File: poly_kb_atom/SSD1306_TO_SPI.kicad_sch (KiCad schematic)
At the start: 12 parts

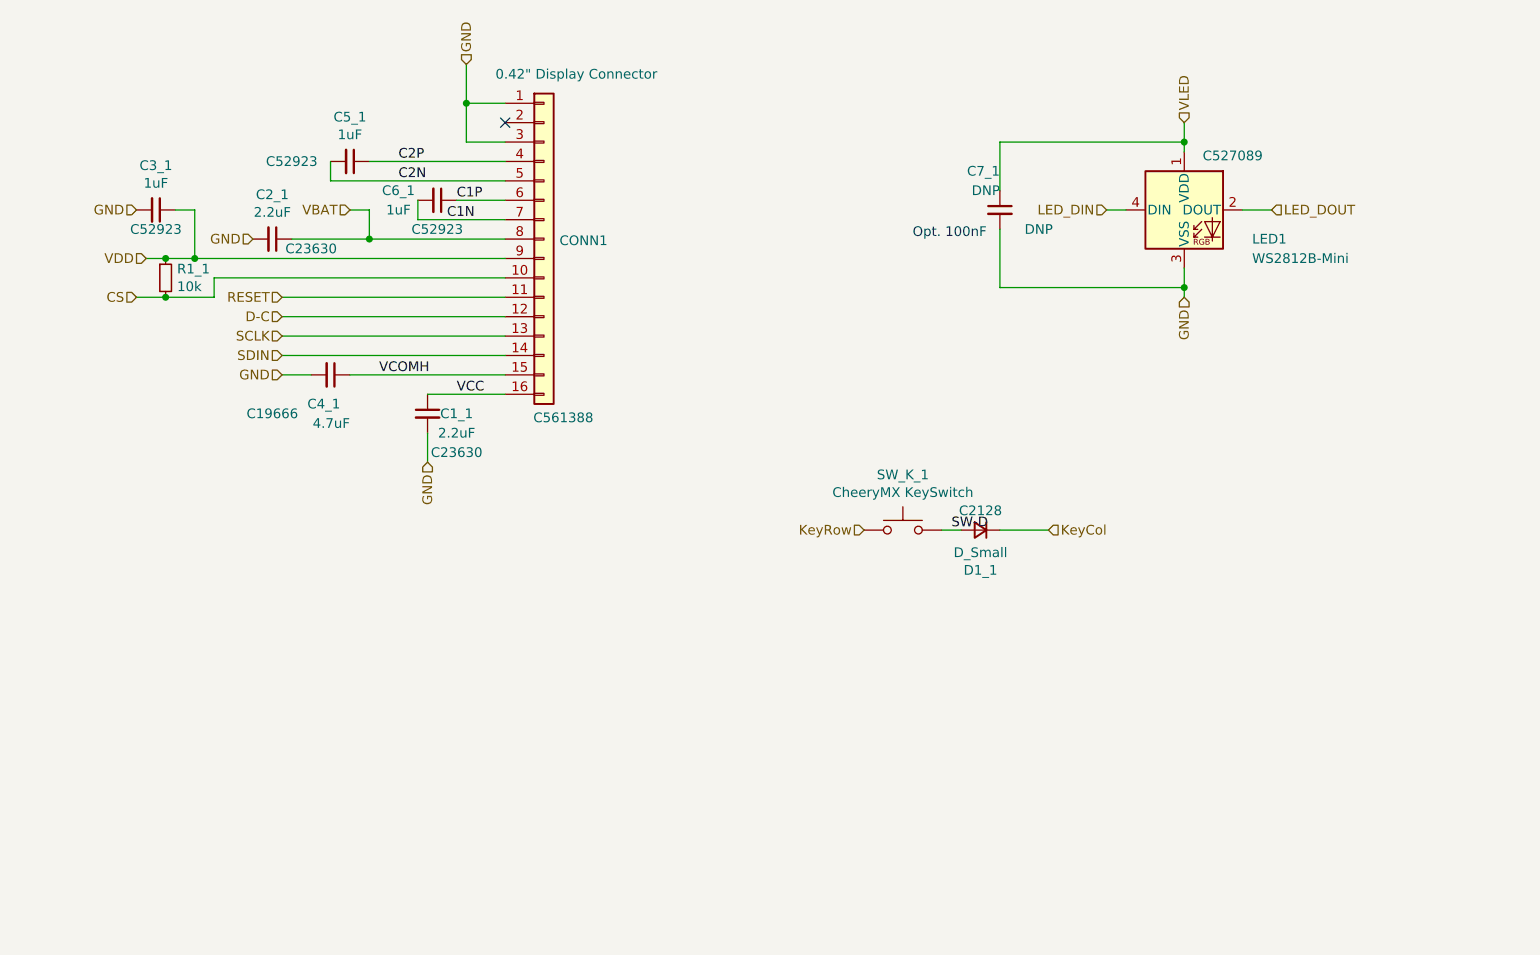
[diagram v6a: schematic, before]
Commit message: Updated WaveL to Revision 1.1
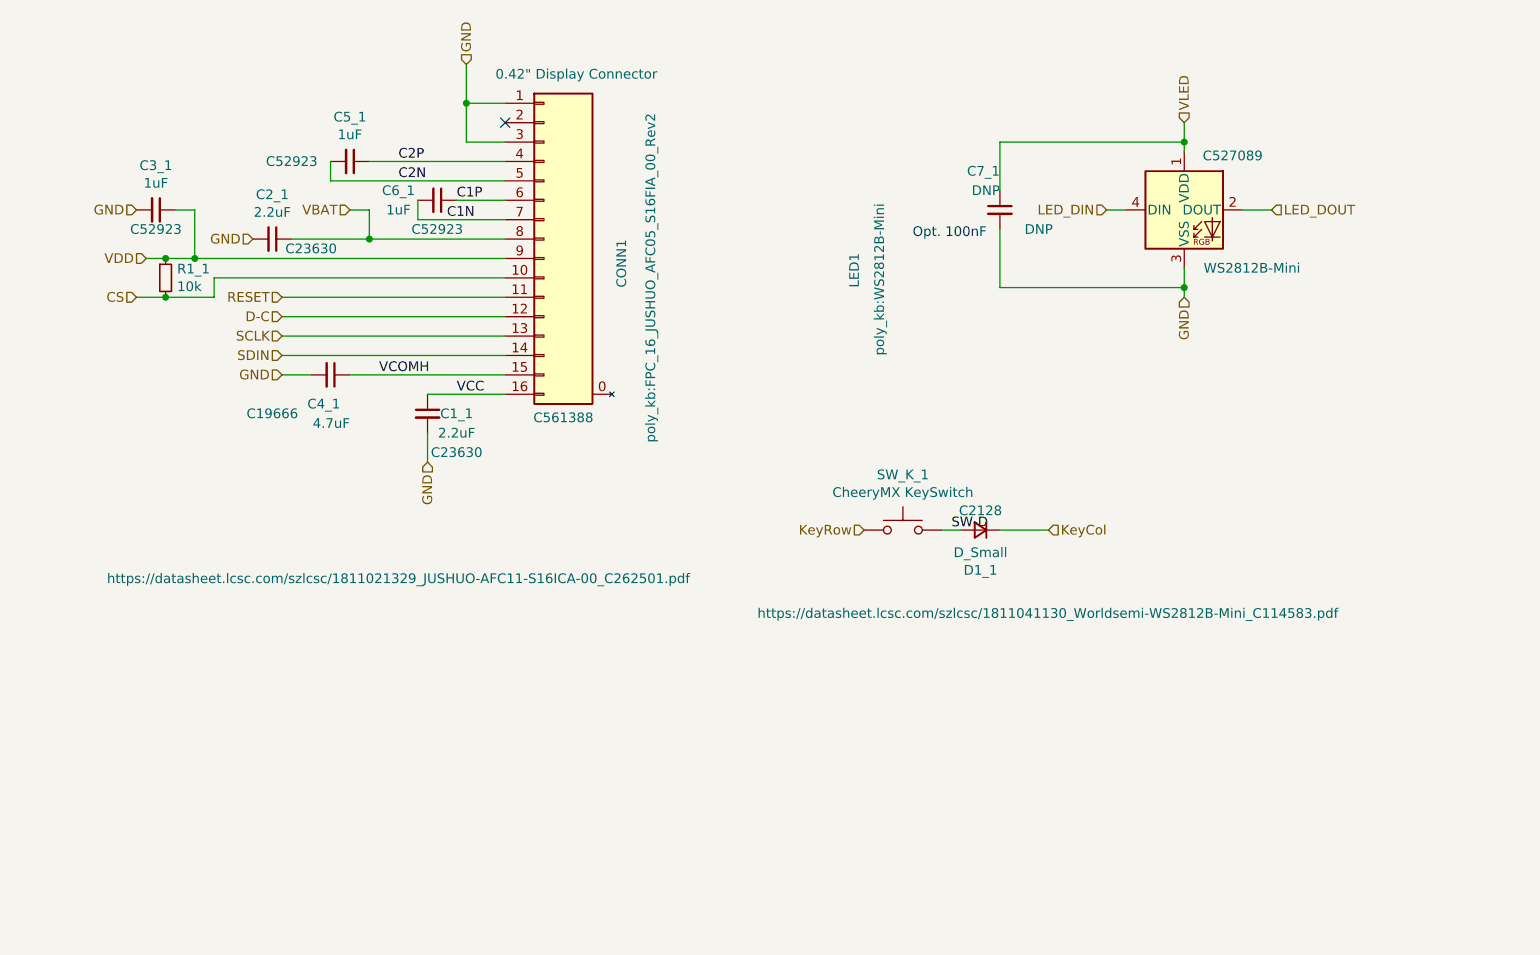
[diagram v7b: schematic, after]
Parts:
- C1_1, C2_1, C4_1, C7_1: footprint (none) -> Capacitor_SMD:C_0603_1608Metric
- C3_1, C5_1, C6_1: footprint (none) -> Capacitor_SMD:C_0402_1005Metric
- CONN1: footprint (none) -> poly_kb:FPC_16_JUSHUO_AFC05_S16FIA_00_Rev2
- D1_1: footprint (none) -> poly_kb:D_SOD-323Ext
- LED1: footprint (none) -> poly_kb:WS2812B-Mini
- R1_1: footprint (none) -> Resistor_SMD:R_0402_1005Metric
- SW_K_1: footprint (none) -> poly_kb:SW_Cherry_MX_1.00u_PCB_NoSilk
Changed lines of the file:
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@@
   (symbol (lib_id "Connector_Generic:Conn_01x16") (at 82.55 52.07 0) (unit 1)
     (in_bom yes) (on_board yes)
-    (property "Reference" "CONN1" (id 0) (at 84.582 52.2732 0)
+    (property "Reference" "CONN1" (id 0) (at 92.71 58.42 90)
       (effects (font (size 1.27 1.27)) (justify left))
     )
@@
       (effects (font (size 1.27 1.27)) (justify left))
     )
-    (property "Footprint" "" (id 2) (at 82.55 52.07 0)
-      (effects (font (size 1.27 1.27)) hide)
-    )
-    (property "Datasheet" "https://datasheet.lcsc.com/szlcsc/1811021329_JUSHUO-AFC11-S16ICA-00_C262501.pdf" (id 3) (at 82.55 52.07 0)
-      (effects (font (size 1.27 1.27)) hide)
-    )
+    (property "Footprint" "poly_kb:FPC_16_JUSHUO_AFC05_S16FIA_00_Rev2" (id 2) (at 96.52 57.15 90))
+    (property "Datasheet" "https://datasheet.lcsc.com/szlcsc/1811021329_JUSHUO-AFC11-S16ICA-00_C262501.pdf" (id 3) (at 63.5 96.52 0))
     (property "LCSC" "C561388" (id 4) (at 85.09 76.2 0)
       (effects (font (size 1.27 1.27)) (justify bottom))
@@
       (effects (font (size 1.27 1.27)) hide)
     )
+    (pin "0")
     (pin "1")
     (pin "10")
@@
     (property "Reference" "C6_1" (id 0) (at 63.5 45.72 90))
     (property "Value" "1uF" (id 1) (at 63.5 48.26 90))
-    (property "Footprint" "" (id 2) (at 68.58 46.99 0)
+    (property "Footprint" "Capacitor_SMD:C_0402_1005Metric" (id 2) (at 68.58 46.99 0)
       (effects (font (size 1.27 1.27)) hide)
     )
@@
   (symbol (lib_id "LED:WS2812B") (at 166.37 48.26 0) (unit 1)
     (in_bom yes) (on_board yes)
-    (property "Reference" "LED1" (id 0) (at 175.26 52.07 0)
-      (effects (font (size 1.27 1.27)) (justify left))
-    )
-    (property "Value" "WS2812B-Mini" (id 1) (at 175.26 54.61 0)
-      (effects (font (size 1.27 1.27)) (justify left))
-    )
-    (property "Footprint" "" (id 2) (at 167.64 55.88 0)
-      (effects (font (size 1.27 1.27)) (justify left top) hide)
-    )
-    (property "Datasheet" "https://datasheet.lcsc.com/szlcsc/1811041130_Worldsemi-WS2812B-Mini_C114583.pdf" (id 3) (at 168.91 57.785 0)
-      (effects (font (size 1.27 1.27)) (justify left top) hide)
+    (property "Reference" "LED1" (id 0) (at 123.19 58.42 90)
+      (effects (font (size 1.27 1.27)) (justify left))
+    )
+    (property "Value" "WS2812B-Mini" (id 1) (at 168.91 55.88 0)
+      (effects (font (size 1.27 1.27)) (justify left))
+    )
+    (property "Footprint" "poly_kb:WS2812B-Mini" (id 2) (at 125.73 67.31 90)
+      (effects (font (size 1.27 1.27)) (justify left top))
+    )
+    (property "Datasheet" "https://datasheet.lcsc.com/szlcsc/1811041130_Worldsemi-WS2812B-Mini_C114583.pdf" (id 3) (at 110.49 100.33 0)
+      (effects (font (size 1.27 1.27)) (justify left top))
     )
     (property "LCSC" "C527089" (id 4) (at 172.72 41.91 0)
@@
       (effects (font (size 1.27 1.27)) (justify right))
     )
-    (property "Footprint" "" (id 2) (at 54.61 69.85 0)
+    (property "Footprint" "Capacitor_SMD:C_0603_1608Metric" (id 2) (at 54.61 69.85 0)
       (effects (font (size 1.27 1.27)) hide)
     )
@@
     (property "Reference" "C1_1" (id 0) (at 71.12 74.93 0))
     (property "Value" "2.2uF" (id 1) (at 71.12 77.47 0))
-    (property "Footprint" "" (id 2) (at 67.31 74.93 0)
+    (property "Footprint" "Capacitor_SMD:C_0603_1608Metric" (id 2) (at 67.31 74.93 0)
       (effects (font (size 1.27 1.27)) hide)
     )
@@
     (property "Reference" "C5_1" (id 0) (at 57.15 36.0934 90))
     (property "Value" "1uF" (id 1) (at 57.15 38.4048 90))
-    (property "Footprint" "" (id 2) (at 57.15 41.91 0)
+    (property "Footprint" "Capacitor_SMD:C_0402_1005Metric" (id 2) (at 57.15 41.91 0)
       (effects (font (size 1.27 1.27)) hide)
     )
@@
     (property "Reference" "C2_1" (id 0) (at 46.99 46.2534 90))
     (property "Value" "2.2uF" (id 1) (at 46.99 48.5648 90))
-    (property "Footprint" "" (id 2) (at 46.99 52.07 0)
+    (property "Footprint" "Capacitor_SMD:C_0603_1608Metric" (id 2) (at 46.99 52.07 0)
       (effects (font (size 1.27 1.27)) hide)
     )
@@
     (property "Reference" "C3_1" (id 0) (at 31.75 42.4434 90))
     (property "Value" "1uF" (id 1) (at 31.75 44.7548 90))
-    (property "Footprint" "" (id 2) (at 31.75 48.26 0)
+    (property "Footprint" "Capacitor_SMD:C_0402_1005Metric" (id 2) (at 31.75 48.26 0)
       (effects (font (size 1.27 1.27)) hide)
     )
@@
     (property "Reference" "SW_K_1" (id 0) (at 129.54 82.931 0))
     (property "Value" "CheeryMX KeySwitch" (id 1) (at 129.54 85.2424 0))
-    (property "Footprint" "" (id 2) (at 129.54 85.09 0)
+    (property "Footprint" "poly_kb:SW_Cherry_MX_1.00u_PCB_NoSilk" (id 2) (at 129.54 85.09 0)
       (effects (font (size 1.27 1.27)) hide)
     )
@@
     (property "Reference" "D1_1" (id 0) (at 139.7 95.4278 0))
     (property "Value" "D_Small" (id 1) (at 139.7 93.1164 0))
-    (property "Footprint" "" (id 2) (at 139.7 90.17 90)
+    (property "Footprint" "poly_kb:D_SOD-323Ext" (id 2) (at 139.7 90.17 90)
       (effects (font (size 1.27 1.27)) hide)
     )
@@
       (effects (font (size 1.27 1.27)) (justify right))
     )
-    (property "Footprint" "" (id 2) (at 142.24 48.26 0)
+    (property "Footprint" "Capacitor_SMD:C_0603_1608Metric" (id 2) (at 142.24 48.26 0)
       (effects (font (size 1.27 1.27)) hide)
     )
@@
       (effects (font (size 1.27 1.27)) (justify left))
     )
-    (property "Footprint" "" (id 2) (at 33.02 57.15 0)
-      (effects (font (size 1.27 1.27)) hide)
-    )
+    (property "Footprint" "Resistor_SMD:R_0402_1005Metric" (id 2) (at 33.02 57.15 0)
+      (effects (font (size 1.27 1.27)) hide)
+    )

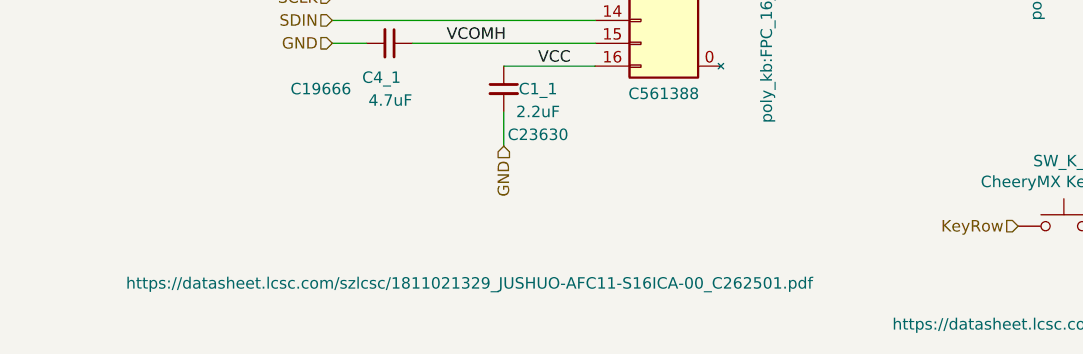
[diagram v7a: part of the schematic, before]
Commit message: Optional termination resistors
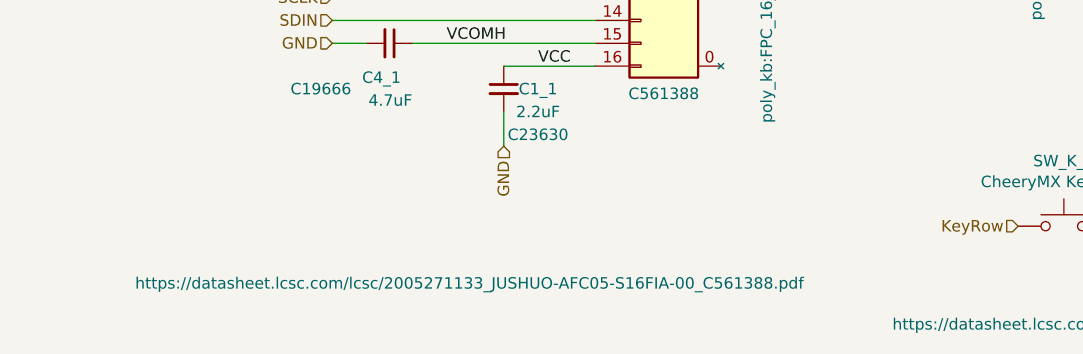
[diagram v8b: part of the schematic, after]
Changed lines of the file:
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@@
     )
     (property "Footprint" "poly_kb:FPC_16_JUSHUO_AFC05_S16FIA_00_Rev2" (id 2) (at 96.52 57.15 90))
-    (property "Datasheet" "https://datasheet.lcsc.com/szlcsc/1811021329_JUSHUO-AFC11-S16ICA-00_C262501.pdf" (id 3) (at 63.5 96.52 0))
+    (property "Datasheet" "https://datasheet.lcsc.com/lcsc/2005271133_JUSHUO-AFC05-S16FIA-00_C561388.pdf" (id 3) (at 63.5 96.52 0))
     (property "LCSC" "C561388" (id 4) (at 85.09 76.2 0)
       (effects (font (size 1.27 1.27)) (justify bottom))
